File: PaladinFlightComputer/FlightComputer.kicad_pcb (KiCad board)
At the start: 4 copper layers, 44.9 x 59.5 mm, 21 parts, among them J1 Micro_SD_Card_Det1, J8 Conn_01x04, U1 GY-521

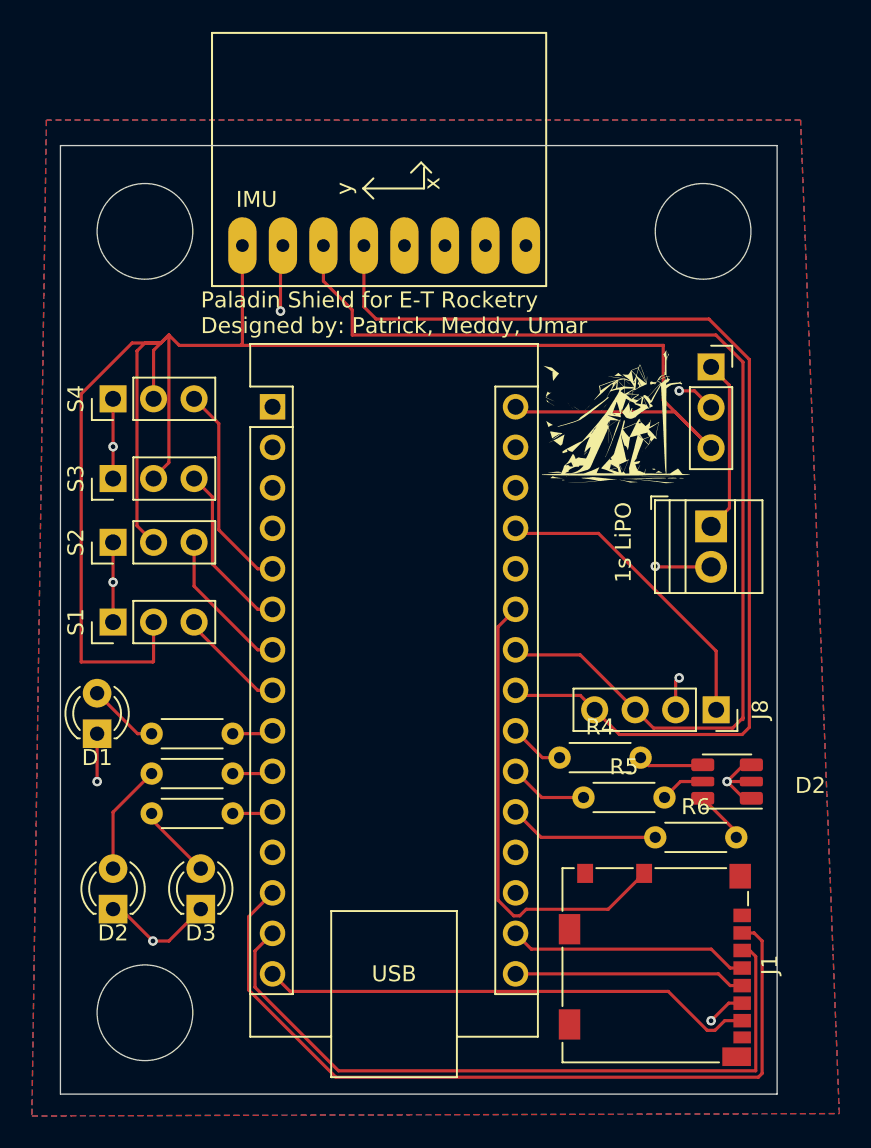
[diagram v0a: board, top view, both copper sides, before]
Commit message: dual rgb lights on both sides
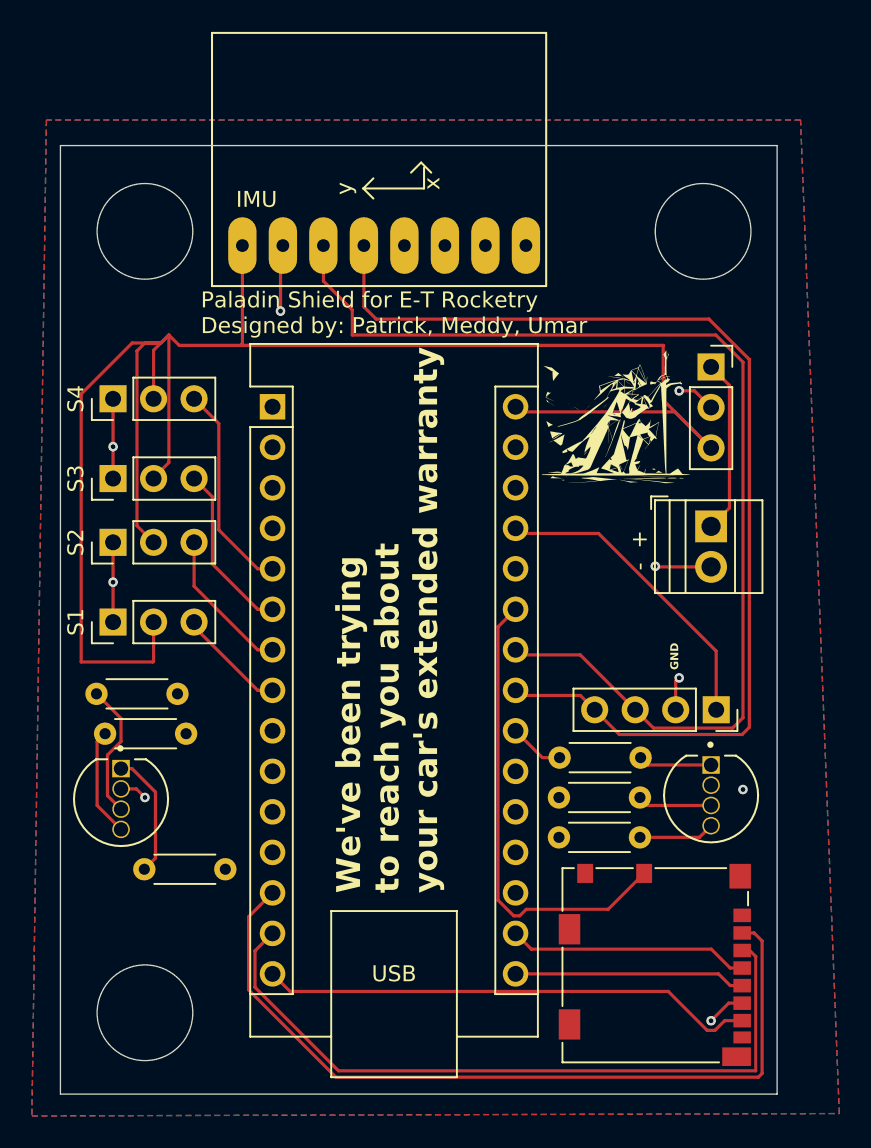
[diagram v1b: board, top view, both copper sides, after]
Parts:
- removed D1, D3: LED, LED_THT:LED_D3.0mm
- removed the D2 at (119.5, 121.5)
- removed the D2 at (81.0, 129.5)
- added D2: WP154A4SUREQBFZGC, WP154A4SUREQBFZGC:LED_WP154A4SUREQBFZGC, F.Cu at (118.5, 122.4)
- added D5: WP154A4SUREQBFZGC, WP154A4SUREQBFZGC:LED_WP154A4SUREQBFZGC, F.Cu at (81.5, 122.6)
- -  +: renamed from 1s LiPO
- J7, R1, R2: renamed from  
- moved R2 6.08 mm to (85.0, 116.0)
- moved R6 6.04 mm to (109.0, 125.0)
- moved R3 3.53 mm to (88.0, 127.0)
- moved R1 2.92 mm to (85.6, 118.5)
- moved R5 1.54 mm to (109.0, 122.5)
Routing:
- net GND: track 40.2 -> 26.4 mm, vias 10 -> 9
- net Net-(A1-A1): track 9.42 -> 0.00 mm
- net Net-(A1-A2): track 4.94 -> 0.00 mm
- net Net-(D5-Pad1): track 4.74 -> 7.90 mm
- net Net-(A1-D6): track 2.77 -> 0.00 mm
- net Net-(A1-D7): track 2.73 -> 0.00 mm
- net Net-(A1-D8): track 2.54 -> 0.00 mm
- net Net-(D5-Pad4): track 4.47 -> 6.83 mm
- net Net-(D2-Pad3): track 2.81 -> 4.67 mm
- net Net-(D5-Pad3): track 6.96 -> 8.57 mm
- net Net-(D2-Pad4): track 3.32 -> 4.76 mm
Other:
- board text added: "GND"
- board text added: "We've been trying to reach you about your car's extended warranty"
